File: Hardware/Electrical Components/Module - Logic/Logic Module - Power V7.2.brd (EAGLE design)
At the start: 65 x 70 mm, 16 parts

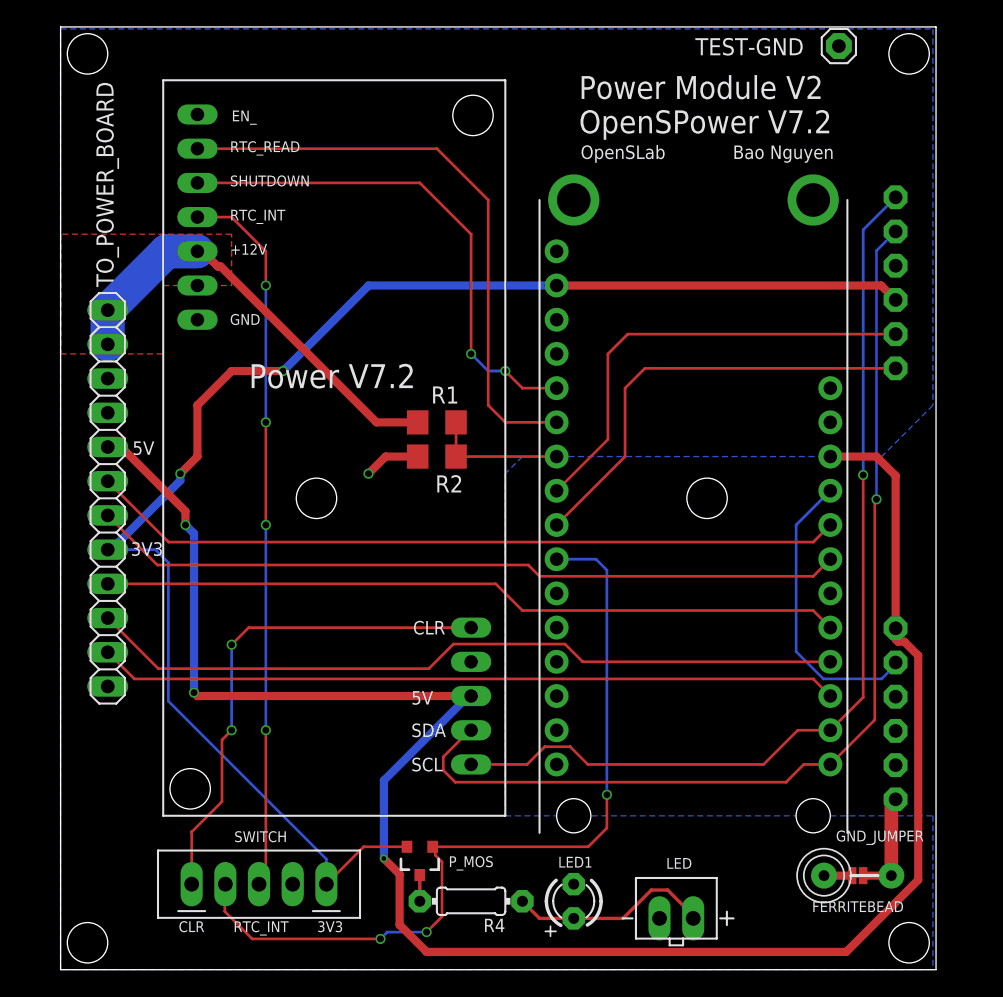
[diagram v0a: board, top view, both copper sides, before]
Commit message: Major fix for sensor module
O Power Module: Changes in footprint location of motor push-to-connect for mounting place. Move the 90-angle header further inside for better mechanical support
O Sensor Module: Rearrange 2.5mm headphone jack closer to the edge for proper mounting. The older version stops the male jack fully dock with the female casing thus fail to connect. Move the 90-angle header further inside for better mechanical support.
O MS5803-02BA: Change symbol, change SDA -> SDO. This label caused the PCB to stop working with all I2C devices. Sensor Module: Rewire to the write SDA, tested.
+ Add MS5803-02BA Datasheet
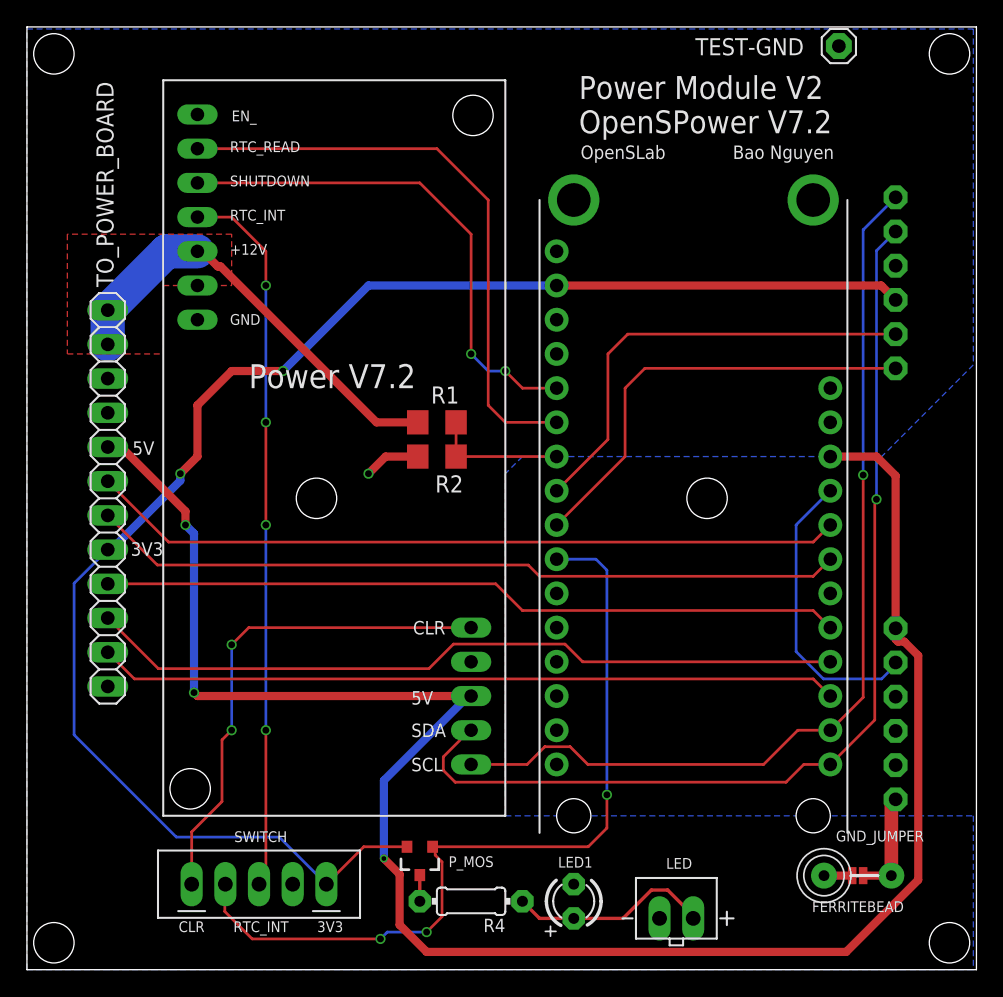
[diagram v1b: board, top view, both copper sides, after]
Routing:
- net +3V3: track 110.4 -> 114.8 mm
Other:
- board size 65 x 70 mm -> 70.5 x 70 mm
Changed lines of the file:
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@@
 <setting verticaltext="up"/>
 </settings>
-<grid distance="50" unitdist="mil" unit="mm" style="lines" multiple="1" display="no" altdistance="5" altunitdist="mil" altunit="mm"/>
+<grid distance="0.5" unitdist="mm" unit="mm" style="lines" multiple="1" display="no" altdistance="5" altunitdist="mil" altunit="mm"/>
 <layers>
 <layer number="1" name="Top" color="4" fill="1" visible="yes" active="yes"/>
@@
 <board>
 <plain>
-<wire x1="0" y1="0" x2="65" y2="0" width="0" layer="20"/>
-<wire x1="65" y1="0" x2="65" y2="70" width="0" layer="20"/>
-<wire x1="65" y1="70" x2="0" y2="70" width="0" layer="20"/>
-<wire x1="0" y1="70" x2="0" y2="0" width="0" layer="20"/>
-<hole x="2" y="2" drill="3"/>
-<hole x="2" y="68" drill="3"/>
-<hole x="63" y="68" drill="3"/>
-<hole x="63" y="2" drill="3"/>
+<wire x1="-2.5" y1="0" x2="68" y2="0" width="0" layer="20"/>
+<wire x1="68" y1="0" x2="68" y2="70" width="0" layer="20"/>
+<wire x1="68" y1="70" x2="-2.5" y2="70" width="0" layer="20"/>
+<wire x1="-2.5" y1="70" x2="-2.5" y2="0" width="0" layer="20"/>
+<hole x="-0.5" y="2" drill="3"/>
+<hole x="-0.5" y="68" drill="3"/>
+<hole x="66" y="68" drill="3"/>
+<hole x="66" y="2" drill="3"/>
 <text x="19.05" y="2.794" size="0.8" layer="21">3V3</text>
 <text x="8.763" y="2.794" size="0.8" layer="21">CLR</text>
@@
 <wire x1="16.51" y1="44.45" x2="22.86" y2="50.8" width="0.6096" layer="16"/>
 <wire x1="22.86" y1="50.8" x2="36.83" y2="50.8" width="0.6096" layer="16"/>
-<wire x1="3.5" y1="31.19" x2="7.037" y2="31.19" width="0.2032" layer="16"/>
-<wire x1="7.037" y1="31.19" x2="8.001" y2="30.226" width="0.2032" layer="16"/>
-<wire x1="8.001" y1="30.226" x2="8.001" y2="19.939" width="0.2032" layer="16"/>
-<wire x1="19.732" y1="8.208" x2="19.732" y2="6.35" width="0.2032" layer="16"/>
-<wire x1="8.001" y1="19.939" x2="19.732" y2="8.208" width="0.2032" layer="16"/>
+<wire x1="3.5" y1="31.19" x2="1.001" y2="28.691" width="0.2032" layer="16"/>
+<wire x1="1.001" y1="28.691" x2="1.001" y2="17.439" width="0.2032" layer="16"/>
+<wire x1="19.732" y1="6.35" x2="16.232" y2="9.85" width="0.2032" layer="16"/>
+<wire x1="16.232" y1="9.85" x2="8.59" y2="9.85" width="0.2032" layer="16"/>
+<wire x1="8.59" y1="9.85" x2="1.001" y2="17.439" width="0.2032" layer="16"/>
 <contactref element="P_MOS" pad="2"/>
 <wire x1="19.732" y1="6.35" x2="22.51" y2="9.128" width="0.2032" layer="1"/>
@@
 <contactref element="TO_POWER_BOARD" pad="4"/>
 <polygon width="0.6096" layer="16">
-<vertex x="0" y="69.85"/>
-<vertex x="64.77" y="69.85"/>
-<vertex x="64.77" y="41.91"/>
+<vertex x="-2.5" y="69.85"/>
+<vertex x="67.77" y="69.85"/>
+<vertex x="67.77" y="44.91"/>
 <vertex x="60.96" y="38.1"/>
 <vertex x="34.29" y="38.1"/>
 <vertex x="33.02" y="36.83"/>
 <vertex x="33.02" y="11.43"/>
-<vertex x="57.15" y="11.43"/>
-<vertex x="64.77" y="11.43"/>
-<vertex x="64.77" y="0"/>
-<vertex x="1.27" y="0"/>
-<vertex x="0" y="0"/>
+<vertex x="67.77" y="11.43"/>
+<vertex x="67.77" y="0"/>
+<vertex x="-2.5" y="0"/>
 </polygon>
 <wire x1="26.518" y1="38.1" x2="24.13" y2="38.1" width="0.6096" layer="1"/>
@@
 <polygon width="0.254" layer="1">
 <vertex x="12.7" y="54.61"/>
-<vertex x="0" y="54.61"/>
-<vertex x="0" y="45.72"/>
+<vertex x="0.5" y="54.61"/>
+<vertex x="0.5" y="45.72"/>
 <vertex x="7.62" y="45.72"/>
 <vertex x="7.62" y="50.8"/>
